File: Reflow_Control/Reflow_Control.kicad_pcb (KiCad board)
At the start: 2 copper layers, 100 x 80 mm, 67 parts, among them J1 Conn_5V, J2 Conn_ssr_1, J3 Conn_ssr_2, Q1 BC848, Q2 BC848, Q3 BC848, SW1 SW_Push, SW2 SW_Push, SW3 SW_Push, SW4 SW_Push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

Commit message: added version + creators name
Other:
- board text added: "Edwin Koch & Kerem Yollu"
- board text added: "V 1.0"
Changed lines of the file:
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@@
-(kicad_pcb (version 20171130) (host pcbnew 5.1.5+dfsg1-2build2)
+(kicad_pcb (version 20171130) (host pcbnew 5.0.2+dfsg1-1)
   (general
     (thickness 1.6)
-    (drawings 9)
+    (drawings 11)
     (tracks 361)
     (zones 0)
@@
     (zone_45_only no)
     (trace_min 0.2)
+    (segment_width 0.2)
+    (edge_width 0.15)
     (via_size 0.8)
     (via_drill 0.4)
@@
     (uvia_min_size 0.2)
     (uvia_min_drill 0.1)
-    (edge_width 0.15)
-    (segment_width 0.2)
     (pcb_text_width 0.3)
     (pcb_text_size 1.5 1.5)
@@
     (pad 1 thru_hole circle (at 0 0 90) (size 3.5 3.5) (drill 2.54) (layers *.Cu *.Mask))
   )
+  (gr_text "Edwin Koch & Kerem Yollu" (at 124.968 123.698) (layer F.SilkS)
+    (effects (font (size 1.5 1.5) (thickness 0.3)))
+  )
+  (gr_text "V 1.0" (at 112.776 127.254) (layer F.SilkS)
+    (effects (font (size 1.5 1.5) (thickness 0.3)))
+  )
   (gr_text "Reflow Oven Controller" (at 127.254 119.888) (layer F.SilkS)

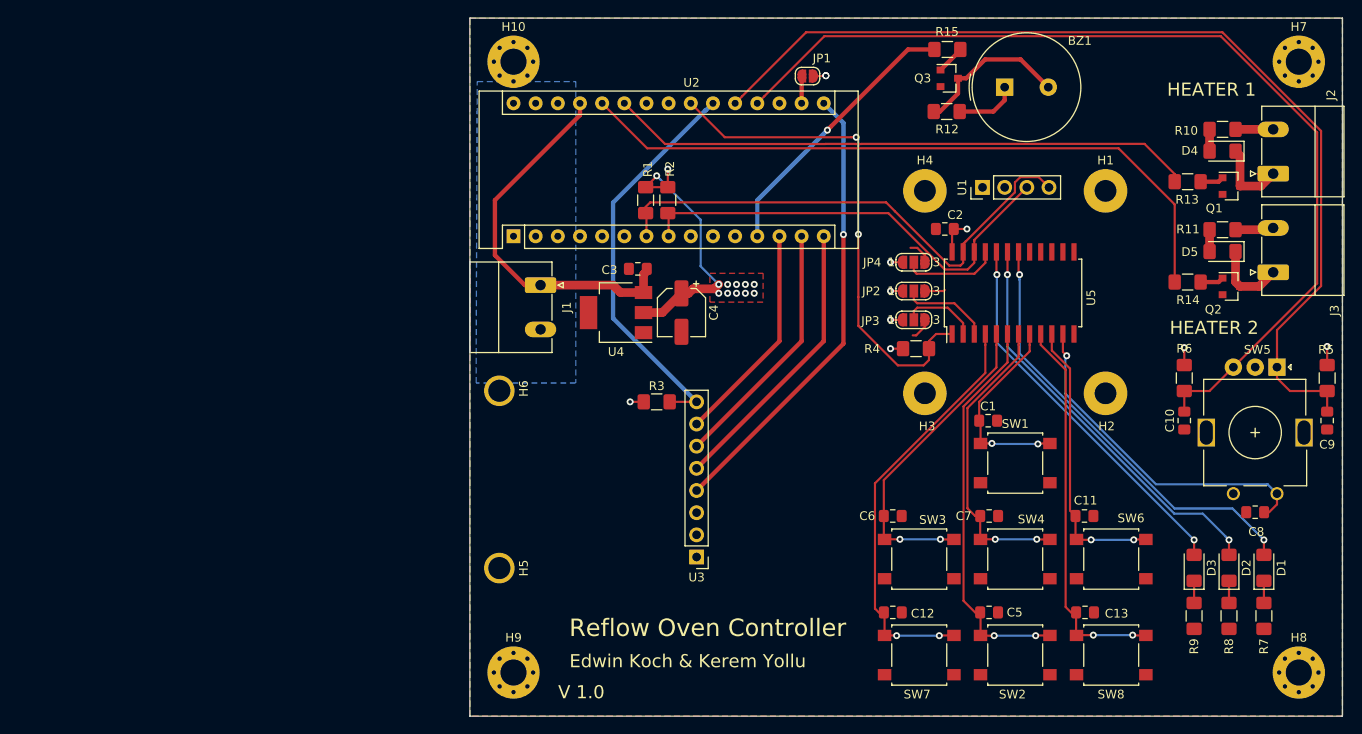
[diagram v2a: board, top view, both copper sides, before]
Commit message: added motor controller
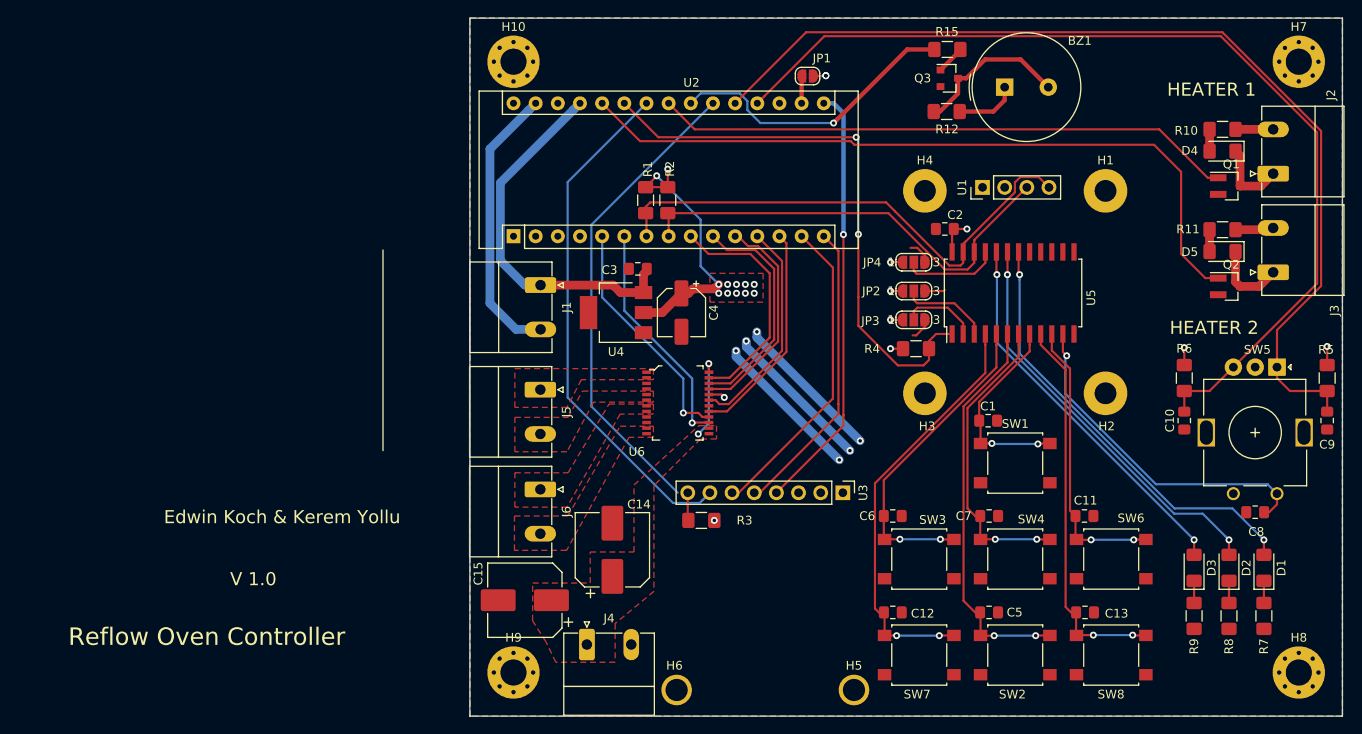
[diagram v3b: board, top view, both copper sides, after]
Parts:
- removed R13, R14: 1k, Resistor_SMD:R_1206_3216Metric_Pad1.42x1.75mm_HandSolder
- added C14: 100uF, Capacitor_SMD:CP_Elec_8x6.2, F.Cu at (116.3, 110.9)
- added C15: 100uF, Capacitor_SMD:CP_Elec_8x6.2, F.Cu at (106.3, 116.7)
- added J4: Conn_mot_PWR, Connector_Phoenix_MC_HighVoltage:PhoenixContact_MC_1,5_2-G-5.08_1x02_P5.08mm_Horizontal, F.Cu at (113.4, 121.8)
- added J5: Conn_mot_1, Connector_Phoenix_MC_HighVoltage:PhoenixContact_MC_1,5_2-G-5.08_1x02_P5.08mm_Horizontal, F.Cu at (108.1, 92.6)
- added J6: Conn_mot_2, Connector_Phoenix_MC_HighVoltage:PhoenixContact_MC_1,5_2-G-5.08_1x02_P5.08mm_Horizontal, F.Cu at (108.1, 104.0)
- added U6: TB6612FNG_C_8_EL, dk_footprints:LSSOP-24_W5.6mm, F.Cu at (123.8, 94.1)
- Q1, Q2: value BC848 -> NUD3112LT1G; footprint Package_TO_SOT_SMD:SOT-23 -> Package_TO_SOT_SMD:SOT-23_Handsoldering
- moved H5 43.0 mm to (144.0, 127.0), turned to 180 degrees
- moved H6 39.9 mm to (123.7, 127.0), turned to 180 degrees
- moved U3 18.3 mm to (142.7, 104.4), turned to 270 degrees
- moved R3 14.5 mm to (126.5, 107.6), turned to 180 degrees
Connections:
- Q1 pad 1: Net-(Q1-Pad1) -> SSR_1
- Q2 pad 1: Net-(Q2-Pad1) -> SSR_2
- U2 pad 10: (no net) -> CH1_MOTOR_IN2
- U2 pad 11: (no net) -> CH1_MOTOR_IN1
- U2 pad 12: TIM1_CH1_PWM_Buzzer -> CH1_MOTOR_STBY
- U2 pad 13: SPI1_CS_MAX31865 -> CH2_MOTOR_IN2
- U2 pad 22: INT_PCA9555 -> TIM1_CH1_PWM_Buzzer
- U2 pad 23: (no net) -> SSR_1
- U2 pad 24: (no net) -> SPI1_CS_MAX31865
- U2 pad 25: TIM3_CH1_HEATER_PWM -> INT_PCA9555
- U2 pad 26: TIM3_CH2_HEATER_PWM -> SSR_2
- U2 pad 5: (no net) -> CH2_MOTOR_IN1
- U2 pad 6: (no net) -> TIM3_CH2_MOTOR_PWM
- U2 pad 9: (no net) -> TIM3_CH1_MOTOR_PWM
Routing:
- net SSR_2: track 0.00 -> 84.4 mm
- net GND: track 7.71 -> 92.1 mm, vias 0 -> 6
- net TIM3_CH2_HEATER_PWM: track 79.3 -> 0.00 mm
- net TIM3_CH1_HEATER_PWM: track 67.3 -> 0.00 mm
- net SSR_1: track 0.00 -> 66.5 mm
- net SPI1_CS_MAX31865: track 25.5 -> 59.3 mm
- net CH2_MOTOR_IN1: track 0.00 -> 27.2 mm, vias 0 -> 1
- net TIM3_CH1_MOTOR_PWM: track 0.00 -> 27.0 mm
- net TIM3_CH2_MOTOR_PWM: track 0.00 -> 26.6 mm, vias 0 -> 1
- net CH1_MOTOR_IN2: track 0.00 -> 26.2 mm
- net CH1_MOTOR_STBY: track 0.00 -> 25.4 mm
- net CH2_MOTOR_IN2: track 0.00 -> 25.3 mm
- net CH1_MOTOR_IN1: track 0.00 -> 25.2 mm
- net INT_MAX31865_RDY: track 46.1 -> 57.6 mm
- net /motor_vcc: track 0.00 -> 9.56 mm, vias 0 -> 2
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- added copper zone on F.Cu, net /motor_vcc
- added copper zone on F.Cu, net Net-(J5-Pad1)
- added copper zone on F.Cu, net Net-(J5-Pad2)
- added copper zone on F.Cu, net Net-(J6-Pad1)
- added copper zone on F.Cu, net Net-(J6-Pad2)
- removed copper zone on B.Cu, net GND

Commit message: reviwewd ground planes connection
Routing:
- net GND: track 92.1 -> 176.0 mm, vias 6 -> 12
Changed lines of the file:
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@@
-(kicad_pcb (version 20171130) (host pcbnew 5.1.5+dfsg1-2build2)
+(kicad_pcb (version 20171130) (host pcbnew 5.0.2+dfsg1-1)
   (general
     (thickness 1.6)
-    (drawings 12)
-    (tracks 439)
+    (drawings 13)
+    (tracks 449)
     (zones 0)
     (modules 71)
@@
   )
   (setup
-    (last_trace_width 1)
+    (last_trace_width 0.5)
     (user_trace_width 0.5)
     (user_trace_width 1)
@@
     (zone_45_only no)
     (trace_min 0.2)
+    (segment_width 0.2)
+    (edge_width 0.15)
     (via_size 0.8)
     (via_drill 0.4)
@@
     (uvia_min_size 0.2)
     (uvia_min_drill 0.1)
-    (edge_width 0.15)
-    (segment_width 0.2)
     (pcb_text_width 0.3)
     (pcb_text_size 1.5 1.5)
@@
     )
   )
-  (gr_line (start 90.043 76.581) (end 90.043 99.568) (layer F.SilkS) (width 0.15))
-  (gr_text "Edwin Koch & Kerem Yollu" (at 78.486 107.188) (layer F.SilkS)
-    (effects (font (size 1.5 1.5) (thickness 0.3)))
+  (gr_text "Edwin Koch & Kerem Yollu" (at 127 54) (layer F.SilkS)
+    (effects (font (size 1 1) (thickness 0.2)))
   )
-  (gr_text "V 1.0" (at 75.184 114.3) (layer F.SilkS)
-    (effects (font (size 1.5 1.5) (thickness 0.3)))
+  (gr_text "V 1.0" (at 113 54) (layer F.SilkS)
+    (effects (font (size 1 1) (thickness 0.2)))
+  )
+  (dimension 80 (width 0.3) (layer B.SilkS)
+    (gr_text "80.000 mm" (at 80.5 90 90) (layer B.SilkS)
+      (effects (font (size 1.5 1.5) (thickness 0.3)))
+    )
+    (feature1 (pts (xy 100 50) (xy 82.013579 50)))
+    (feature2 (pts (xy 100 130) (xy 82.013579 130)))
+    (crossbar (pts (xy 82.6 130) (xy 82.6 50)))
+    (arrow1a (pts (xy 82.6 50) (xy 83.186421 51.126504)))
+    (arrow1b (pts (xy 82.6 50) (xy 82.013579 51.126504)))
+    (arrow2a (pts (xy 82.6 130) (xy 83.186421 128.873496)))
+    (arrow2b (pts (xy 82.6 130) (xy 82.013579 128.873496)))
+  )
+  (dimension 100.00005 (width 0.3) (layer B.SilkS)
+    (gr_text "100.000 mm" (at 150.0106 39.45021 359.9427042) (layer B.SilkS)
+      (effects (font (size 1.5 1.5) (thickness 0.3)))
+    )
+    (feature1 (pts (xy 200 50.1) (xy 200.009086 41.013789)))
+    (feature2 (pts (xy 100 50) (xy 100.009086 40.913789)))
+    (crossbar (pts (xy 100.0085 41.500209) (xy 200.0085 41.600209)))
+    (arrow1a (pts (xy 200.0085 41.600209) (xy 198.88141 42.185503)))
+    (arrow1b (pts (xy 200.0085 41.600209) (xy 198.882583 41.012662)))
+    (arrow2a (pts (xy 100.0085 41.500209) (xy 101.134417 42.087756)))
+    (arrow2b (pts (xy 100.0085 41.500209) (xy 101.13559 40.914915)))
   )
-  (gr_text "Reflow Oven Controller" (at 69.85 120.904) (layer F.SilkS)
+  (gr_text "Reflow Oven Controller" (at 128 52) (layer F.SilkS)
     (effects (font (size 2 2) (thickness 0.3)))
   )
@@
   (segment (start 102.29999 82.67999) (end 102.29999 65.00001) (width 1) (layer B.Cu) (net 3))
   (segment (start 108.1 85.68) (end 105.3 85.68) (width 1) (layer B.Cu) (net 3) (status 10))
-  (via (at 132.8928 85.9536) (size 0.8) (drill 0.4) (layers F.Cu B.Cu) (net 3))
-  (via (at 131.6736 87.0204) (size 0.8) (drill 0.4) (layers F.Cu B.Cu) (net 3))
-  (via (at 130.5052 88.138) (size 0.8) (drill 0.4) (layers F.Cu B.Cu) (net 3))
-  (via (at 142.3416 100.6348) (size 0.8) (drill 0.4) (layers F.Cu B.Cu) (net 3))
-  (via (at 144.7292 98.4504) (size 0.8) (drill 0.4) (layers F.Cu B.Cu) (net 3))
-  (via (at 143.5608 99.568) (size 0.8) (drill 0.4) (layers F.Cu B.Cu) (net 3))
-  (segment (start 132.8928 86.614) (end 144.7292 98.4504) (width 1) (layer B.Cu) (net 3))
-  (segment (start 132.8928 85.9536) (end 132.8928 86.614) (width 1) (layer B.Cu) (net 3))
-  (segment (start 131.6736 87.6808) (end 143.5608 99.568) (width 1) (layer B.Cu) (net 3))
-  (segment (start 131.6736 87.0204) (end 131.6736 87.6808) (width 1) (layer B.Cu) (net 3))
-  (segment (start 130.5052 88.7984) (end 142.3416 100.6348) (width 1) (layer B.Cu) (net 3))
-  (segment (start 130.5052 88.138) (end 130.5052 88.7984) (width 1) (layer B.Cu) (net 3))
+  (via (at 172 101) (size 0.8) (drill 0.4) (layers F.Cu B.Cu) (net 3))
+  (via (at 172 102) (size 0.8) (drill 0.4) (layers F.Cu B.Cu) (net 3))
+  (via (at 172 103) (size 0.8) (drill 0.4) (layers F.Cu B.Cu) (net 3))
+  (via (at 145 103) (size 0.8) (drill 0.4) (layers F.Cu B.Cu) (net 3))
+  (via (at 145 102) (size 0.8) (drill 0.4) (layers F.Cu B.Cu) (net 3))
+  (via (at 145 101) (size 0.8) (drill 0.4) (layers F.Cu B.Cu) (net 3))
+  (segment (start 146 102) (end 172 102) (width 0.5) (layer B.Cu) (net 3))
+  (segment (start 146 103) (end 172 103) (width 0.5) (layer B.Cu) (net 3))
+  (via (at 130 88) (size 0.8) (drill 0.4) (layers F.Cu B.Cu) (net 3))
+  (via (at 131 87) (size 0.8) (drill 0.4) (layers F.Cu B.Cu) (net 3))
+  (via (at 143 101) (size 0.8) (drill 0.4) (layers F.Cu B.Cu) (net 3))
+  (via (at 144 100) (size 0.8) (drill 0.4) (layers F.Cu B.Cu) (net 3))
+  (via (at 145 99) (size 0.8) (drill 0.4) (layers F.Cu B.Cu) (net 3))
+  (via (at 132 86) (size 0.8) (drill 0.4) (layers F.Cu B.Cu) (net 3))
+  (segment (start 144.29999 98.29999) (end 132 86) (width 0.5) (layer B.Cu) (net 3))
+  (segment (start 144 100) (end 131 87) (width 0.5) (layer B.Cu) (net 3))
+  (segment (start 143 101) (end 130 88) (width 0.5) (layer B.Cu) (net 3))
+  (segment (start 145 99) (end 144.29999 98.29999) (width 0.5) (layer B.Cu) (net 3))
+  (segment (start 145 103) (end 146 103) (width 0.5) (layer B.Cu) (net 3))
+  (segment (start 146 102) (end 145 102) (width 0.5) (layer B.Cu) (net 3))
+  (segment (start 171 101) (end 172 101) (width 0.5) (layer B.Cu) (net 3))
+  (segment (start 145 101) (end 171 101) (width 0.5) (layer B.Cu) (net 3))
   (segment (start 158.525 96.6) (end 158.605 96.52) (width 0.25) (layer F.Cu) (net 4) (status 30))
   (segment (start 158.525 98.75) (end 158.525 96.6) (width 0.25) (layer F.Cu) (net 4) (status 30))
@@
     (polygon
       (pts
-        (xy 121.031 95.377) (xy 117.221 95.377) (xy 111.125 106.045) (xy 105.156 106.045) (xy 105.156 102.108)
-        (xy 111.252 102.108) (xy 115.951 94.234) (xy 121.031 94.234)
+        (xy 121.005 95.3) (xy 117.195 95.3) (xy 111.125 106.045) (xy 105.156 106.045) (xy 105.156 102.108)
+        (xy 111.252 102.108) (xy 115.96 94.3) (xy 121.04 94.3)
       )
     )
